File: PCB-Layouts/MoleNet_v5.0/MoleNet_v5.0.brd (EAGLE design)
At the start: 100 x 80 mm, 53 parts, among them J3 693072010801, Q1 MOSFET-NCHANNELBSS138, U1 STM32L073RZT6, U2 SN74LVC1G240DBVR, U3 MCP1703-1802E/DB, X1 8MHz, X2 32kHz, X3 R141426

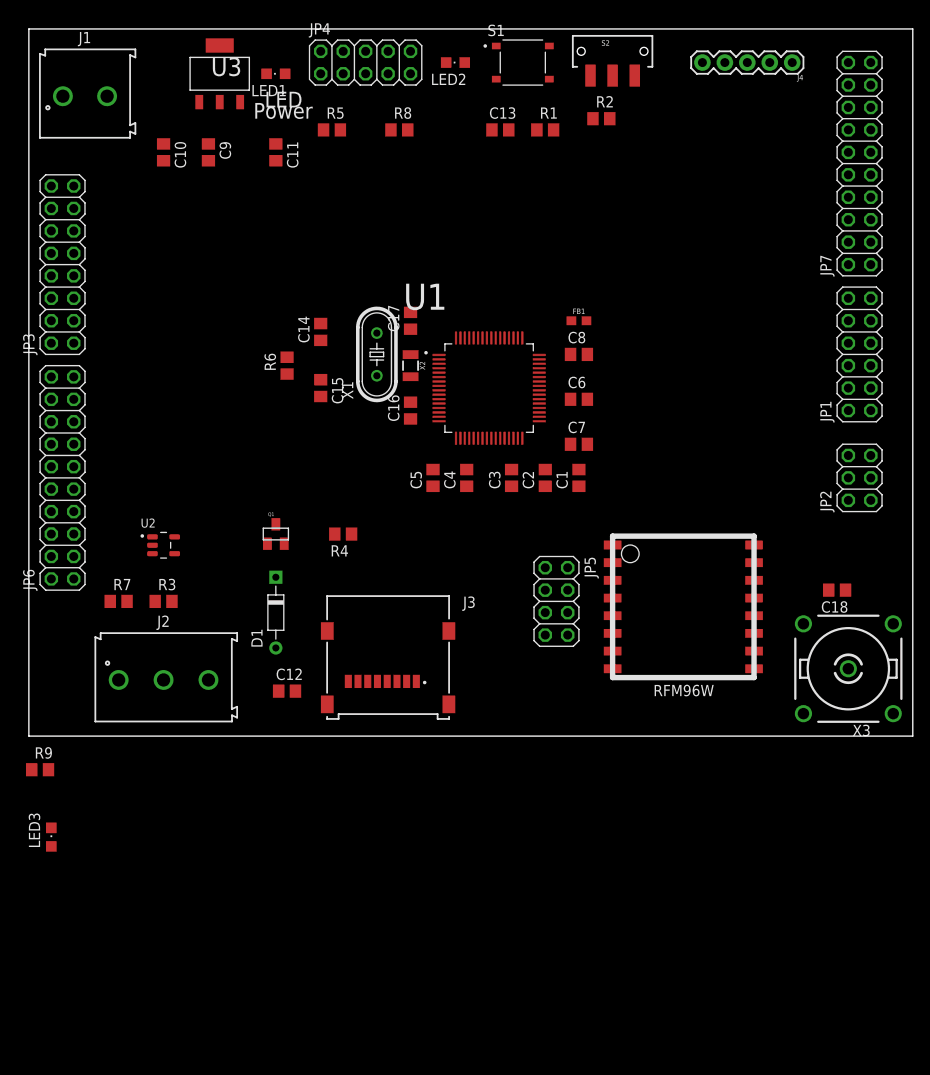
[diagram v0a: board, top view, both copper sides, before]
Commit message: componens inconsistency errors fixed, components on PCB arranged
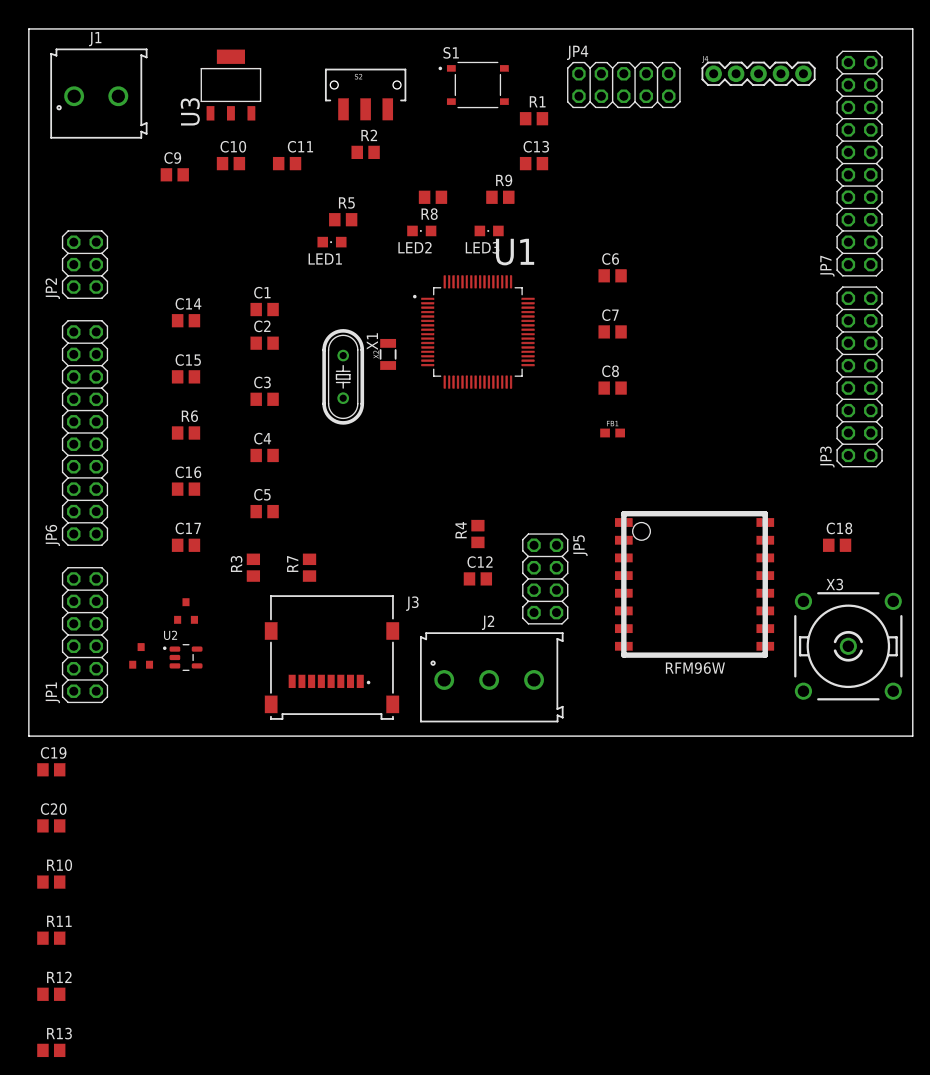
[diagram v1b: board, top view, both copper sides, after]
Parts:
- removed D1: BZX55B15-TAP, Diodes-2:DO-35
- removed Q1: MOSFET-NCHANNELBSS138, BeagleBone_Blue_R3:SOT23
- added C19: 1uF, rcl:C0805
- added C20: 10uF, rcl:C0805
- added R10, R11, R12, R13: 10K, resistor:R0805
- added U$32: BSS123LT1G_STYLE-21, BSS123LT1G:BZX84C7V5LT1G
- added U$34: BZX84C7V5LT1G_STYLE-8, BZX84C7V5LT1G:BZX84C7V5LT1G
- moved JP1 93.2 mm to (6.35, 11.4)
- moved JP3 91.1 mm to (94.0, 40.6)
- moved JP2 90.9 mm to (6.35, 53.3)
- moved LED3 84.6 mm to (52.1, 57.1), turned to 90 degrees
- moved R9 83.1 mm to (53.3, 61.0)
- moved C1 40.3 mm to (26.7, 48.3), turned to 0 degrees
- moved J2 36.8 mm to (52.1, 6.35)
- moved C17 35.9 mm to (17.8, 21.6), turned to 0 degrees
- moved C2 35.2 mm to (26.7, 44.5), turned to 0 degrees
- moved JP4 29.3 mm to (67.3, 73.7)
- moved C3 29.3 mm to (26.7, 38.1), turned to 0 degrees
- moved S2 28.2 mm to (38.1, 73.7)
- moved R2 26.9 mm to (38.1, 66.0)
- moved C16 26.9 mm to (17.8, 27.9), turned to 0 degrees
- moved C12 25.0 mm to (50.8, 17.8)
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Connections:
- removed net LED2: LED2.A, U1.57
- new net N$11: R4.2, U$32.P$3
- new net PB5: R9.2, U1.57
- net 3.3V: now also C19.1, C20.1, R10.2, R11.2, R12.2, R13.2, R5.2; no longer LED1.A
- net GND: now also C19.2, C20.2, LED1.C, LED2.C, LED3.C, U$32.P$2, U$34.P$1; no longer D1.A, Q1.2, R5.1, R8.1, R9.1
- net N$2: now also U$34.P$3; no longer D1.C
- net N$3: now also U$32.P$1; no longer Q1.1
- net N$7: now also LED1.A, R5.1; no longer LED1.C, R5.2
- net N$8: now also LED2.A, R8.1; no longer LED2.C, R8.2
- net N$9: now also LED3.A, R9.1; no longer LED3.C, R9.2
- net SD_CS: now also R12.1
- net SD_MISO: now also J3.8, R13.1; no longer J3.7
- net SD_MOSI: now also R11.1
- net SD_SCK: now also R10.1
- net SWDIO: now also R8.2
- net USART1_RX: no longer Q1.3, R4.2
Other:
- board text removed: "LED"
- board text removed: "Power"

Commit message: ERC errors and warnings are fixed
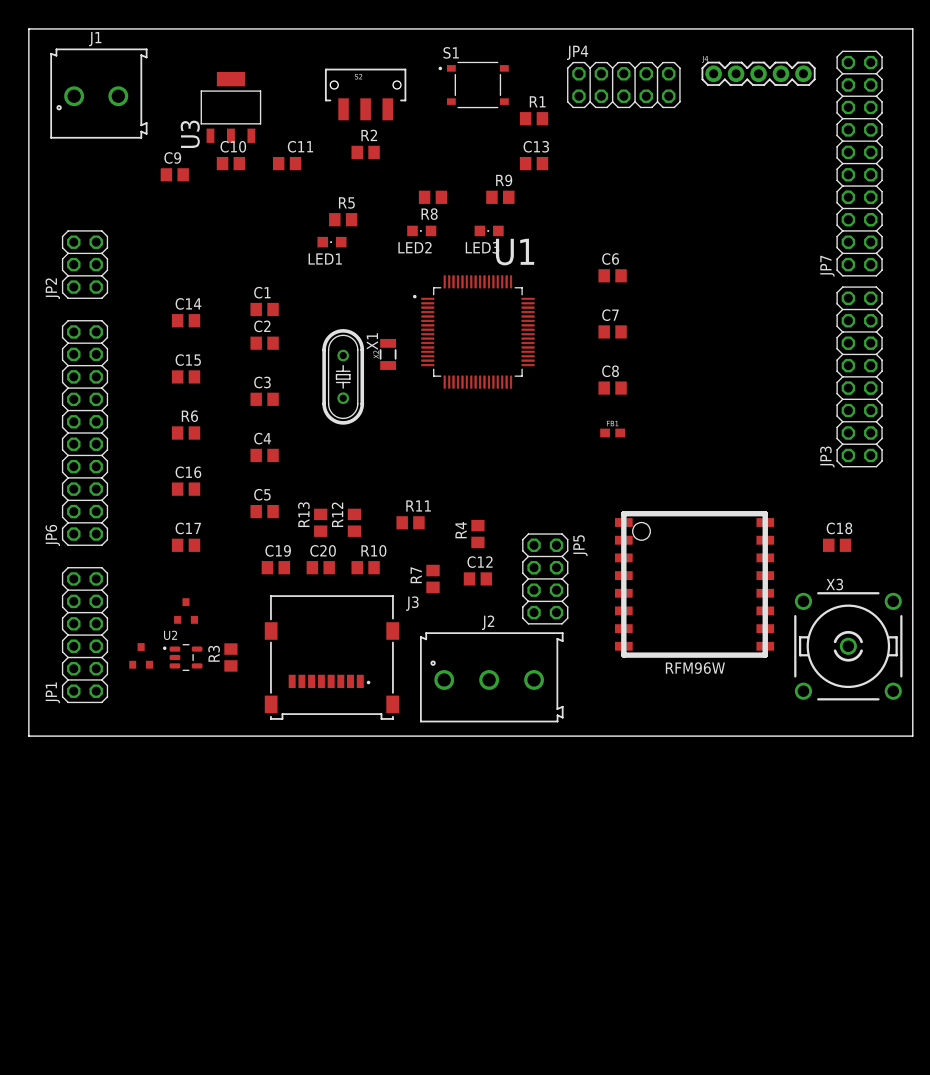
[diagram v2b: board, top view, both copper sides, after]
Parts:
- moved R13 67.0 mm to (33.0, 24.1), turned to 90 degrees
- moved R12 63.4 mm to (36.8, 24.1), turned to 90 degrees
- moved R11 62.1 mm to (43.2, 24.1)
- moved R10 50.3 mm to (38.1, 19.1)
- moved C20 42.2 mm to (33.0, 19.1)
- moved C19 34.2 mm to (27.9, 19.1)
- moved R7 14.0 mm to (45.7, 17.8)
- moved R3 10.5 mm to (22.9, 8.89)
- moved U3 2.54 mm to (22.9, 71.1)
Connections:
- removed net N$11: R4.2, U$32.P$3
- removed net N$19: U1.54
- removed net PC6: JP7.3, U1.37
- removed net USART1_CK: U1.41
- net 3.3V: now also JP7.3
- net DIR_OUT: now also U1.41
- net PD2: now also U1.54
- net RFM_RX/TX: now also U1.37
- net USART1_RX: now also R4.2, U$32.P$3

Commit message: a KiCad design file added, named MoleNet_v5.01
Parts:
- moved LED2 37.0 mm to (76.2, 76.2)
- moved C17 34.5 mm to (38.1, 49.5), turned to 180 degrees
- moved R8 32.6 mm to (76.2, 72.4)
- moved C16 27.9 mm to (38.1, 47.0), turned to 180 degrees
- moved LED1 16.9 mm to (30.5, 72.4), turned to 270 degrees
- moved J4 11.7 mm to (85.1, 66.0), turned to 90 degrees
- moved R5 11.4 mm to (30.5, 68.6)
- moved R1 9.67 mm to (48.3, 66.0), turned to 270 degrees
- moved C9 6.35 mm to (22.9, 63.5), turned to 270 degrees
- moved C13 5.24 mm to (52.1, 66.0), turned to 270 degrees
- moved LED3 5.24 mm to (53.3, 62.2)
- moved C10 5.24 mm to (17.8, 63.5), turned to 270 degrees
- moved X2 5.24 mm to (41.9, 48.3), turned to 270 degrees
- moved R2 4.58 mm to (41.9, 63.5), turned to 180 degrees
- moved X1 3.59 mm to (38.1, 38.1)
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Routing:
- net VIN: track 0.00 -> 114.8 mm
- net SWDIO: track 0.00 -> 35.3 mm
- net SWCLK: track 0.00 -> 26.3 mm
- net BOOT0: track 0.00 -> 14.7 mm
- net NRST: track 0.00 -> 13.7 mm
- net 3.3V: track 0.00 -> 11.0 mm
- net N$1: track 0.00 -> 11.0 mm
- net PB5: track 0.00 -> 9.06 mm
- net OSC32_IN: track 0.00 -> 6.54 mm
- net OSC32_OUT: track 0.00 -> 6.50 mm
- net GND: track 0.00 -> 5.49 mm
- net N$4: track 0.00 -> 5.00 mm
- net N$7: track 0.00 -> 3.85 mm
- net N$8: track 0.00 -> 3.85 mm
- net N$9: track 0.00 -> 2.58 mm
